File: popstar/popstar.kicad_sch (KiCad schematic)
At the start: 1 part, among them U1 ATmega32U4-A

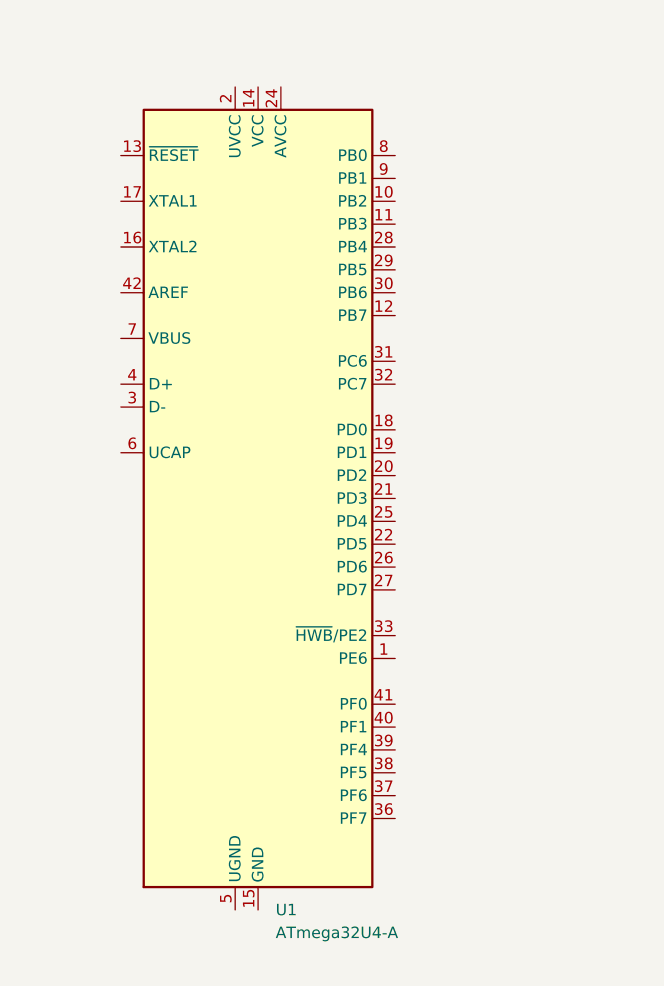
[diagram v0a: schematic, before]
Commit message: Rearranged directories
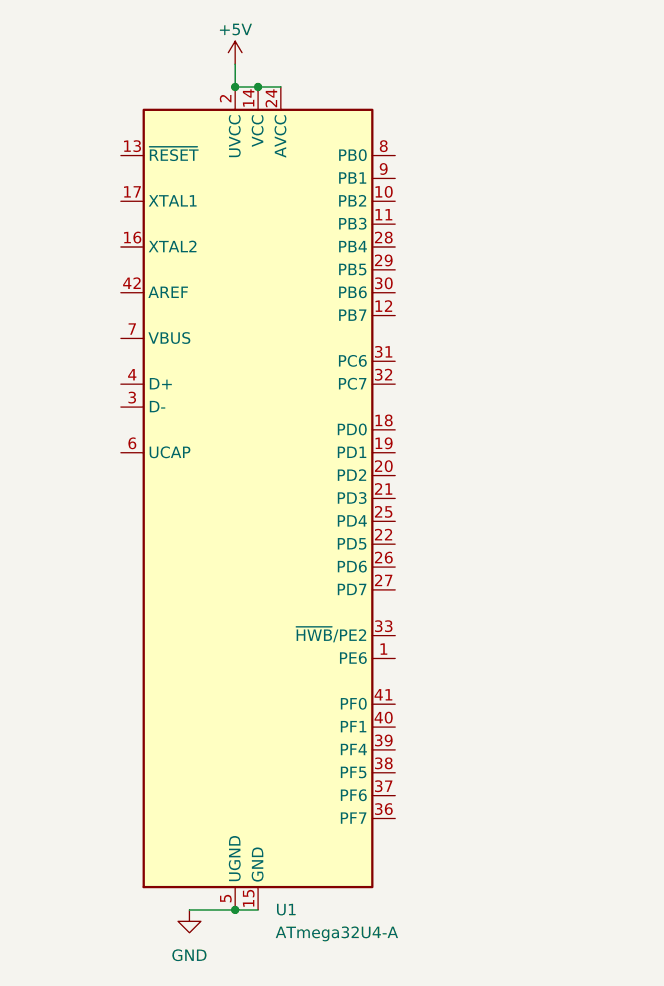
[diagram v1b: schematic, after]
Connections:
- net +5V: now reaches U1.14 (VCC), U1.34 (VCC)
- net +5V: now also U1.2 (UVCC), U1.24 (AVCC), U1.44 (AVCC)
- net GND: now reaches U1.15 (GND), U1.23 (GND), U1.35 (GND), U1.43 (GND)
- net GND: now also U1.5 (UGND)
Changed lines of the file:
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@@
 (kicad_sch (version 20230121) (generator eeschema)
   (paper "A4")
+  (junction (at 48.26 22.86) (diameter 0) (color 0 0 0 0)
+  )
+  (junction (at 50.8 22.86) (diameter 0) (color 0 0 0 0)
+  )
+  (junction (at 48.26 114.3) (diameter 0) (color 0 0 0 0)
+  )
+  (wire (pts (xy 50.8 22.86) (xy 53.34 22.86))
+    (stroke (width 0) (type default))
+  )
+  (wire (pts (xy 48.26 22.86) (xy 50.8 22.86))
+    (stroke (width 0) (type default))
+  )
+  (wire (pts (xy 48.26 114.3) (xy 50.8 114.3))
+    (stroke (width 0) (type default))
+  )
+  (wire (pts (xy 43.18 114.3) (xy 48.26 114.3))
+    (stroke (width 0) (type default))
+  )
+  (wire (pts (xy 48.26 20.32) (xy 48.26 22.86))
+    (stroke (width 0) (type default))
+  )
   (symbol (lib_id "MCU_Microchip_ATmega:ATmega32U4-A") (at 50.8 68.58 0) (unit 1)
     (in_bom yes) (on_board yes) (dnp no) (fields_autoplaced)
@@
         )
       )
+    )
+  )
+  (symbol (lib_id "power:+5V") (at 48.26 20.32 0) (unit 1)
+    (in_bom yes) (on_board yes) (dnp no) (fields_autoplaced)
+    (property "Reference" "#PWR01" (at 48.26 24.13 0)
+      (effects (font (size 1.27 1.27)) hide)
+    )
+    (property "Value" "+5V" (at 48.26 16.51 0)
+      (effects (font (size 1.27 1.27)))
+    )
+    (property "Footprint" "" (at 48.26 20.32 0)
+      (effects (font (size 1.27 1.27)) hide)
+    )
+    (property "Datasheet" "" (at 48.26 20.32 0)
+      (effects (font (size 1.27 1.27)) hide)
+    )
+    (pin "1")
+    (instances
+      (project "popstar"
+        (path "/38a1a9ff-9c00-4248-947e-eb94ab6d8a39"
+          (reference "#PWR01") (unit 1)
+        )
+      )
+    )
+  )
+  (symbol (lib_id "power:GND") (at 43.18 114.3 0) (unit 1)
+    (in_bom yes) (on_board yes) (dnp no) (fields_autoplaced)
+    (property "Reference" "#PWR02" (at 43.18 120.65 0)
+      (effects (font (size 1.27 1.27)) hide)
+    )
+    (property "Value" "GND" (at 43.18 119.38 0)
+      (effects (font (size 1.27 1.27)))
+    )
+    (property "Footprint" "" (at 43.18 114.3 0)
+      (effects (font (size 1.27 1.27)) hide)
+    )
+    (property "Datasheet" "" (at 43.18 114.3 0)
+      (effects (font (size 1.27 1.27)) hide)
+    )
+    (pin "1")
+    (instances
+      (project "popstar"
+        (path "/38a1a9ff-9c00-4248-947e-eb94ab6d8a39"
+          (reference "#PWR02") (unit 1)
+        )
+      )

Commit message: Added RP2040 version of popstar (branched from ice60)
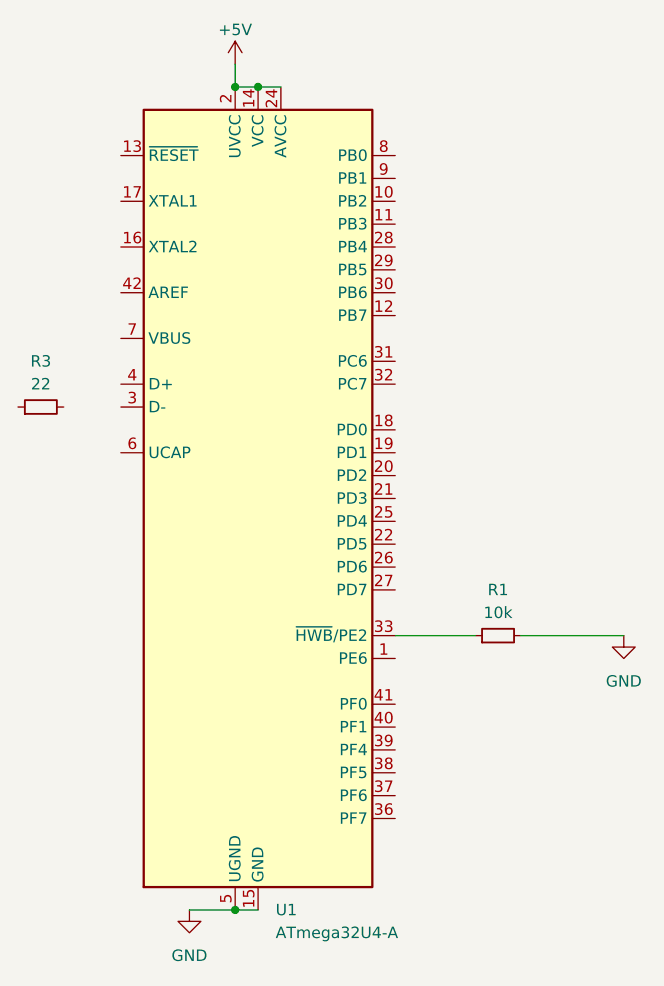
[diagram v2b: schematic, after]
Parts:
- added R1: 10k, symbol Device:R_Small
- added R3: 22, symbol Device:R_Small
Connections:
- net GND: now also R1.2
- net at U1.33 (~{HWB}/PE2): now also R1.1
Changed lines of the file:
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@@
+    (stroke (width 0) (type default))
+  )
+  (wire (pts (xy 66.04 83.82) (xy 74.93 83.82))
     (stroke (width 0) (type default))
   )
   (wire (pts (xy 48.26 114.3) (xy 50.8 114.3))
+    (stroke (width 0) (type default))
+  )
+  (wire (pts (xy 80.01 83.82) (xy 91.44 83.82))
     (stroke (width 0) (type default))
   )
@@
   (wire (pts (xy 48.26 20.32) (xy 48.26 22.86))
     (stroke (width 0) (type default))
+  )
+  (symbol (lib_id "Device:R_Small") (at 77.47 83.82 90) (unit 1)
+    (in_bom yes) (on_board yes) (dnp no) (fields_autoplaced)
+    (property "Reference" "R1" (at 77.47 78.74 90)
+      (effects (font (size 1.27 1.27)))
+    )
+    (property "Value" "10k" (at 77.47 81.28 90)
+      (effects (font (size 1.27 1.27)))
+    )
+    (property "Footprint" "" (at 77.47 83.82 0)
+      (effects (font (size 1.27 1.27)) hide)
+    )
+    (property "Datasheet" "~" (at 77.47 83.82 0)
+      (effects (font (size 1.27 1.27)) hide)
+    )
+    (pin "1")
+    (pin "2")
+    (instances
+      (project "popstar"
+        (path "/38a1a9ff-9c00-4248-947e-eb94ab6d8a39"
+          (reference "R1") (unit 1)
+        )
+      )
+    )
   )
   (symbol (lib_id "MCU_Microchip_ATmega:ATmega32U4-A") (at 50.8 68.58 0) (unit 1)
@@
     )
   )
+  (symbol (lib_id "power:GND") (at 91.44 83.82 0) (unit 1)
+    (in_bom yes) (on_board yes) (dnp no) (fields_autoplaced)
+    (property "Reference" "#PWR03" (at 91.44 90.17 0)
+      (effects (font (size 1.27 1.27)) hide)
+    )
+    (property "Value" "GND" (at 91.44 88.9 0)
+      (effects (font (size 1.27 1.27)))
+    )
+    (property "Footprint" "" (at 91.44 83.82 0)
+      (effects (font (size 1.27 1.27)) hide)
+    )
+    (property "Datasheet" "" (at 91.44 83.82 0)
+      (effects (font (size 1.27 1.27)) hide)
+    )
+    (pin "1")
+    (instances
+      (project "popstar"
+        (path "/38a1a9ff-9c00-4248-947e-eb94ab6d8a39"
+          (reference "#PWR03") (unit 1)
+        )
+      )
+    )
+  )
   (symbol (lib_id "power:+5V") (at 48.26 20.32 0) (unit 1)
     (in_bom yes) (on_board yes) (dnp no) (fields_autoplaced)
@@
         )
       )
+    )
+  )
+  (symbol (lib_id "Device:R_Small") (at 26.67 58.42 90) (unit 1)
+    (in_bom yes) (on_board yes) (dnp no) (fields_autoplaced)
+    (property "Reference" "R3" (at 26.67 53.34 90)
+      (effects (font (size 1.27 1.27)))
+    )
+    (property "Value" "22" (at 26.67 55.88 90)
+      (effects (font (size 1.27 1.27)))
+    )
+    (property "Footprint" "" (at 26.67 58.42 0)
+      (effects (font (size 1.27 1.27)) hide)
+    )
+    (property "Datasheet" "~" (at 26.67 58.42 0)
+      (effects (font (size 1.27 1.27)) hide)
+    )
+    (pin "1")
+    (pin "2")
+    (instances
+      (project "popstar"
+        (path "/38a1a9ff-9c00-4248-947e-eb94ab6d8a39"
+          (reference "R3") (unit 1)
+        )
+      )
